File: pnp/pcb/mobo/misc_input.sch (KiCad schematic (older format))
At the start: 30 parts, among them J18 R_LIMIT, J19 P_LIMIT, J20 C_LIMIT, J60 X_LIMIT, J61 Y_LIMIT, J62 Z_LIMIT, U10 2SMPP-03, U11 LM358, U12 2SMPP-03, U13 INA126, U6 LM358, U9 INA126

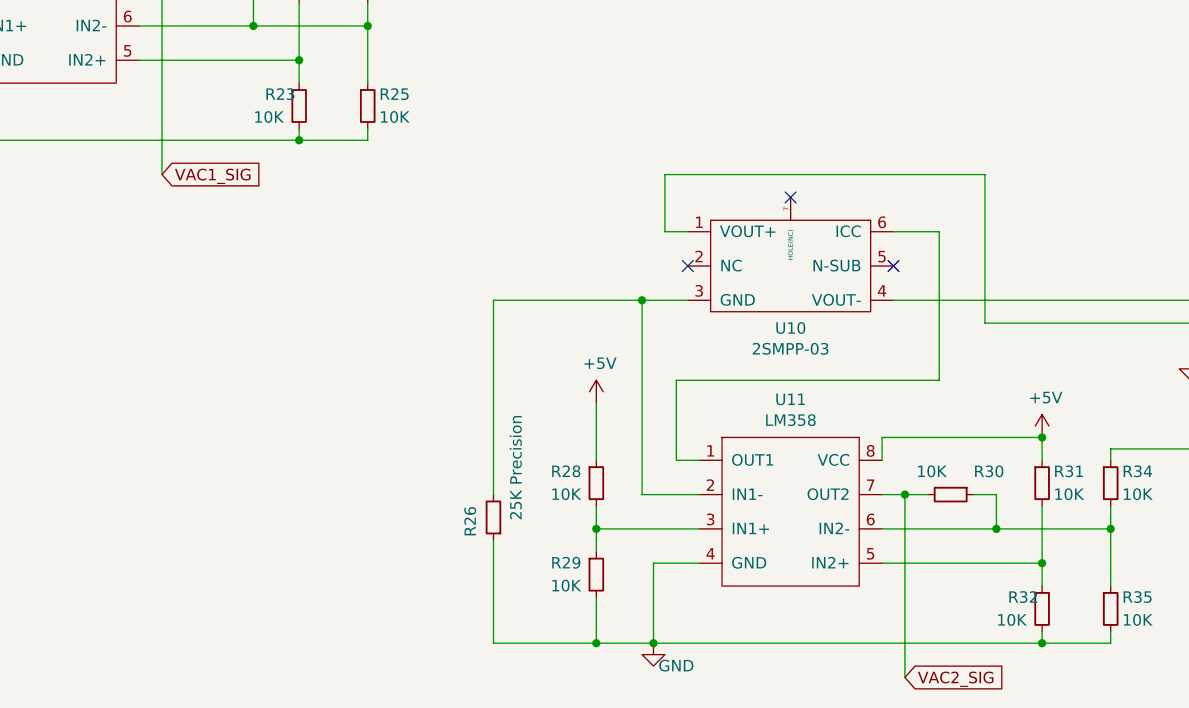
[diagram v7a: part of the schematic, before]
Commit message: fix vacuum sense pin naming to match silkscreen
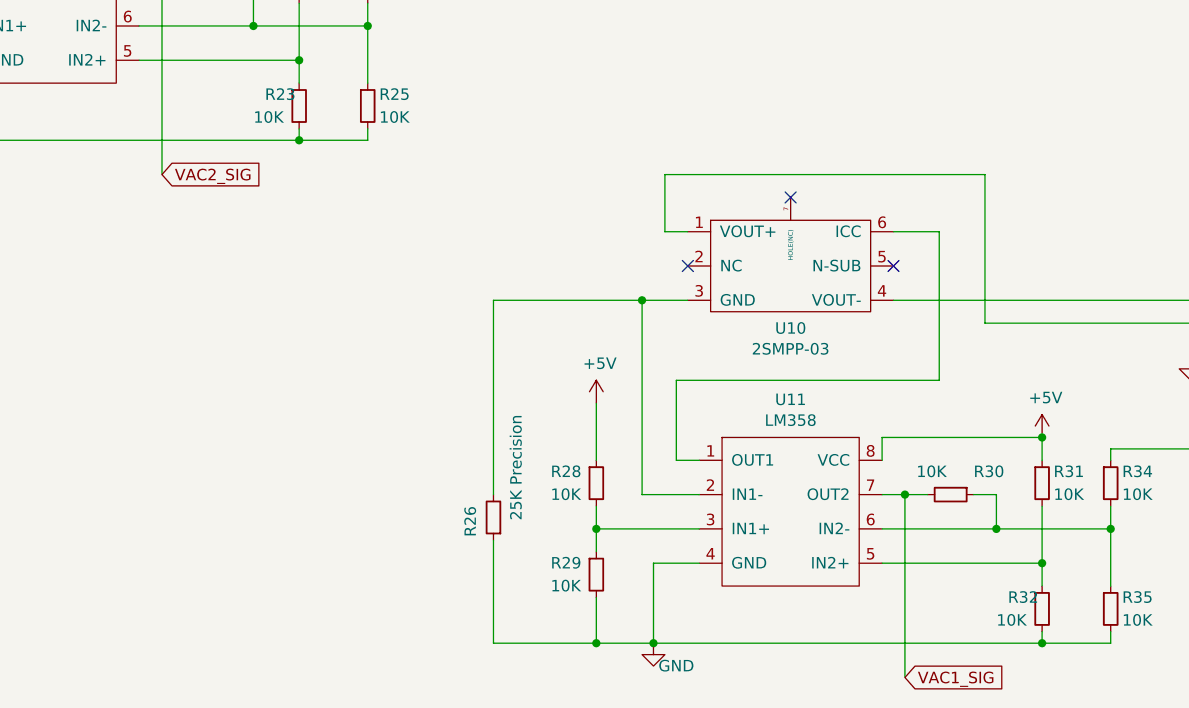
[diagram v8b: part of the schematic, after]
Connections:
- net VAC1_SIG: now also R30.2, U11.7 (OUT2); no longer R22.2, U6.7 (OUT2)
- net VAC2_SIG: now also R22.2, U6.7 (OUT2); no longer R30.2, U11.7 (OUT2)
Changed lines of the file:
@@
 Limit Switches
 Text GLabel 4750 3850 2    50   Input ~ 0
-VAC1_SIG
+VAC2_SIG
 $Comp
 L mobo-rescue:2SMPP-03-index U12
@@
 	5650 2850 6900 2850
 Text GLabel 8000 6050 2    50   Input ~ 0
-VAC2_SIG
+VAC1_SIG
 $Comp
 L mobo-rescue:2SMPP-03-index U10
